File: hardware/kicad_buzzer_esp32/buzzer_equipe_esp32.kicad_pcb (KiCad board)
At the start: 2 copper layers, 110 x 125 mm, 6 parts, among them J2 Module charge TP4056+protect+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, J3 Module vibreur IN/VCC/GND, SW1 Bouton BUZZ (fils volants), SW2 Interrupteur marche/arret (fi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, U1 Vers ESP32 DevKit (module sur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

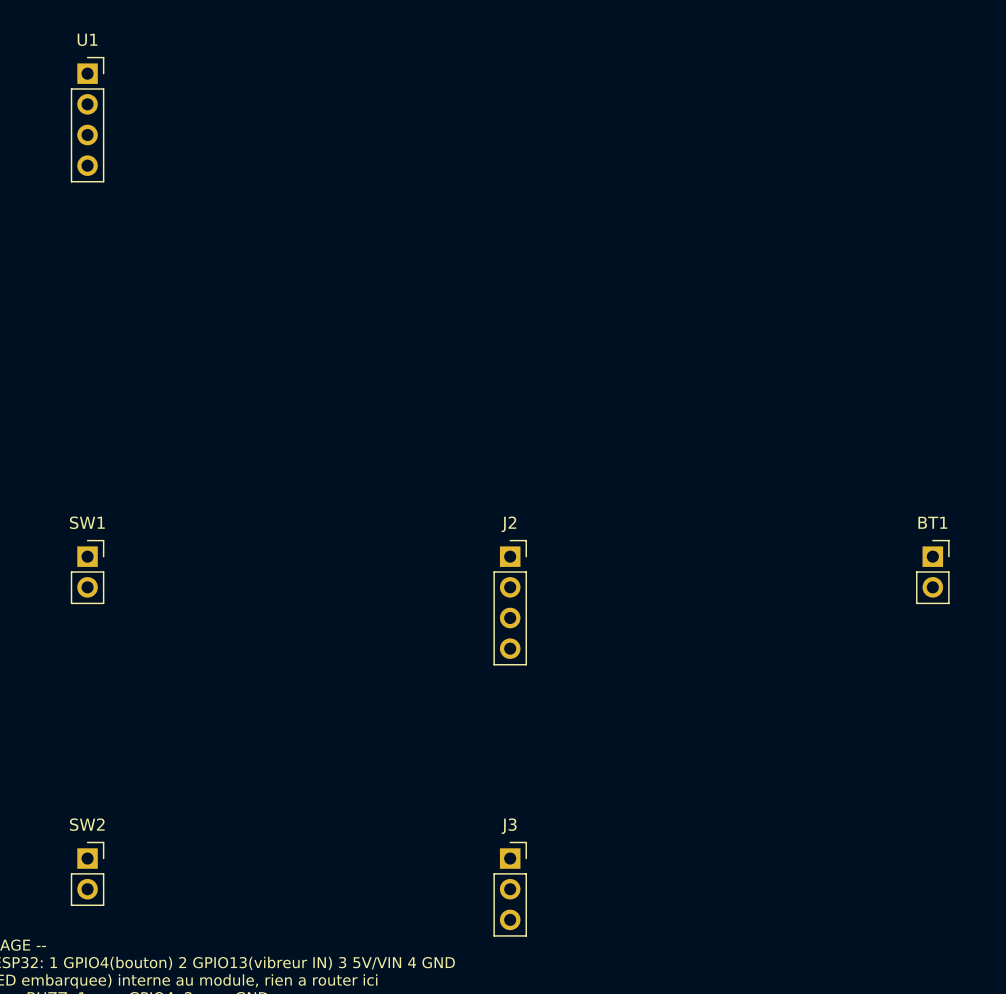
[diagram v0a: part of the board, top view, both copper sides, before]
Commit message: hardware: pistes routees sur les 3 cartes (Freerouting + kicad-cli pcb drc)
Autoroutage headless via Freerouting (pcbnew.ExportSpecctraDSN -> java -jar
freerouting.jar -> pcbnew.ImportSpecctraSES), pas un routage devine a la
main. Resultat verifie avec kicad-cli pcb drc reel sur les 3 cartes: 0
violation de clearance, 0 element non connecte. Seuls avertissements
restants: lib_footprint_mismatch (cosmetique) et quelques track_dangling
(residu mineur d'autorouter, a nettoyer dans KiCad, sans impact electrique).

Co-Authored-By: Claude Sonnet 5 <noreply@anthropic.com>
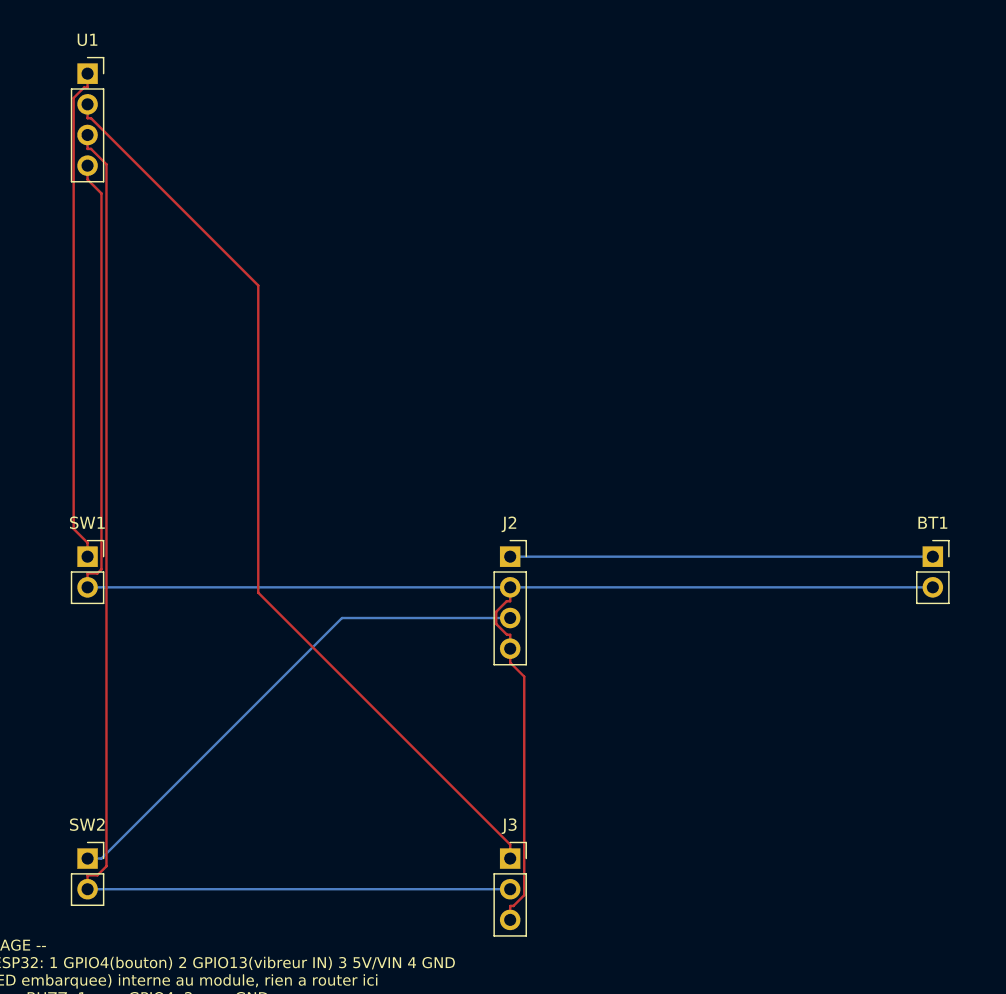
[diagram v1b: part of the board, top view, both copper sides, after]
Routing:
- net GND: track 0.00 -> 136.3 mm
- net VCC_5V_SW: track 0.00 -> 99.4 mm
- net VIBE_IN: track 0.00 -> 77.1 mm
- net VCC_5V_RAW: track 0.00 -> 43.3 mm
- net BTN_SIG: track 0.00 -> 41.1 mm
- net BAT_PLUS: track 0.00 -> 35.0 mm

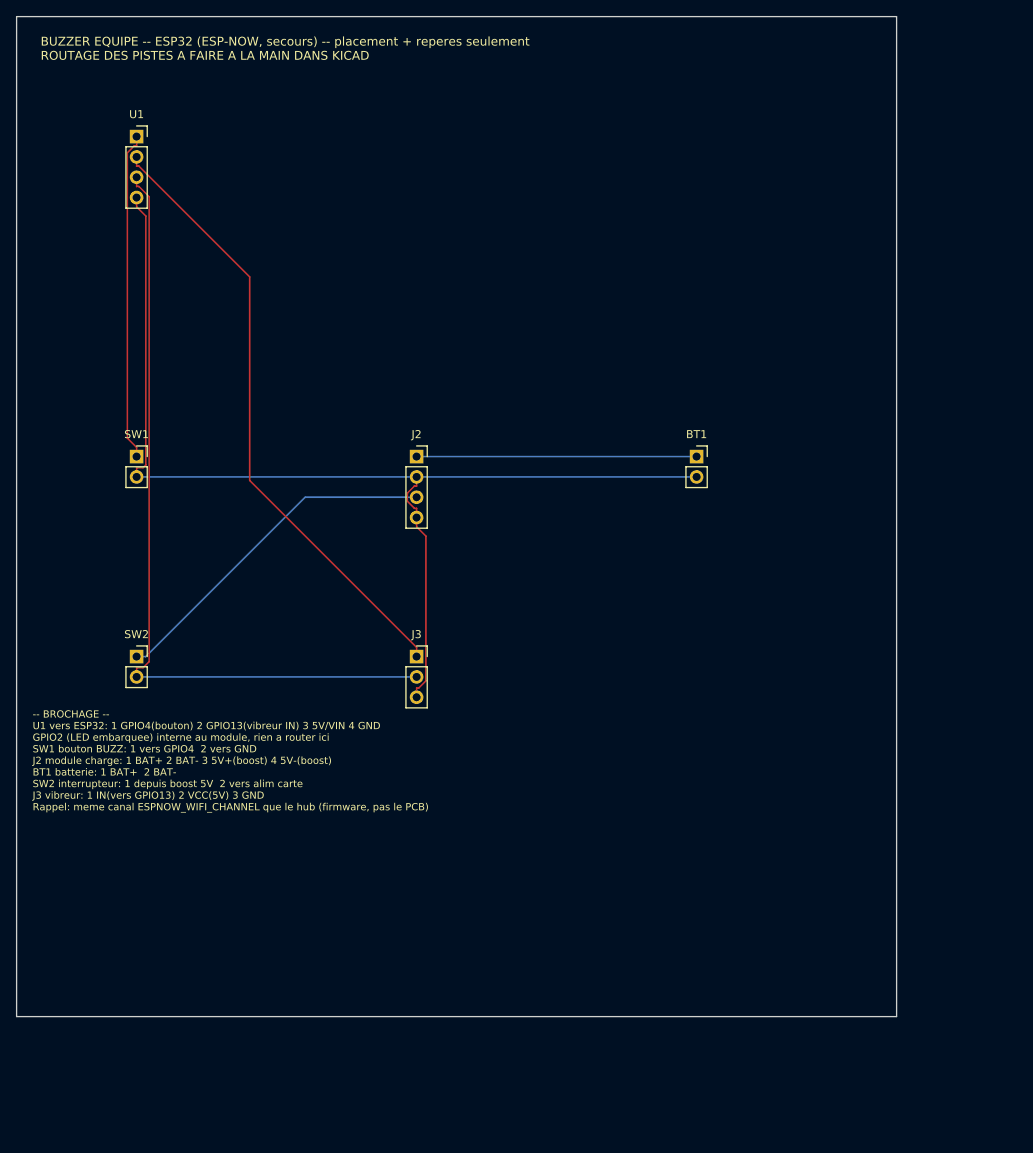
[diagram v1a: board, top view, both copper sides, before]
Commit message: hardware: vrais ports femelles pour les modules (Nano, ESP32 x2) + reroutage
Remplace les empreintes abstraites/simplifiees par de vraies barrettes
femelles PinSocket, dimensionnees et brochees pour correspondre aux modules
physiques reels, sur les 3 cartes:

- Nano (buzzer equipe): 2x PinSocket_1x15 (A1L/A1R, 30 broches, entraxe
  15,24mm) au lieu de l'empreinte "Nano soude directement" -- numerotation
  verifiee contre la vraie empreinte Module:Arduino_Nano.
- ESP32 buzzer (secours): 2x PinSocket_1x19 (U1L/U1R, 38 broches, entraxe
  22,86mm) au lieu du connecteur 4 broches abstrait -- brochage GPIO4/
  GPIO13/VIN/GND positionne selon le layout generique 38 broches le plus
  courant (verifie en ligne), avec avertissement clair dans le README:
  plusieurs variantes de clones existent, a verifier sur le module recu.
- ESP32 hub (regie): 2x PinSocket_1x15 (U_ESP32L/R, 30 broches, entraxe
  15,24mm) au lieu du connecteur 12 broches abstrait -- brochage DOIT ESP32
  DevKit V1 verifie (le modele exact confirme par le client), design de
  reference unique donc plus fiable que les clones 38 broches.

Les 34/19 broches physiques non utilisees sur chaque module restent
presentes sans net (fixation mecanique uniquement). Toutes les cartes
re-routees (Freerouting) et revalidees (kicad-cli pcb drc): 0 violation de
clearance, 0 element non connecte, 0 track_dangling restant (nettoyage
verifie topologie par topologie pour ne pas casser une piste utile).

Co-Authored-By: Claude Sonnet 5 <noreply@anthropic.com>
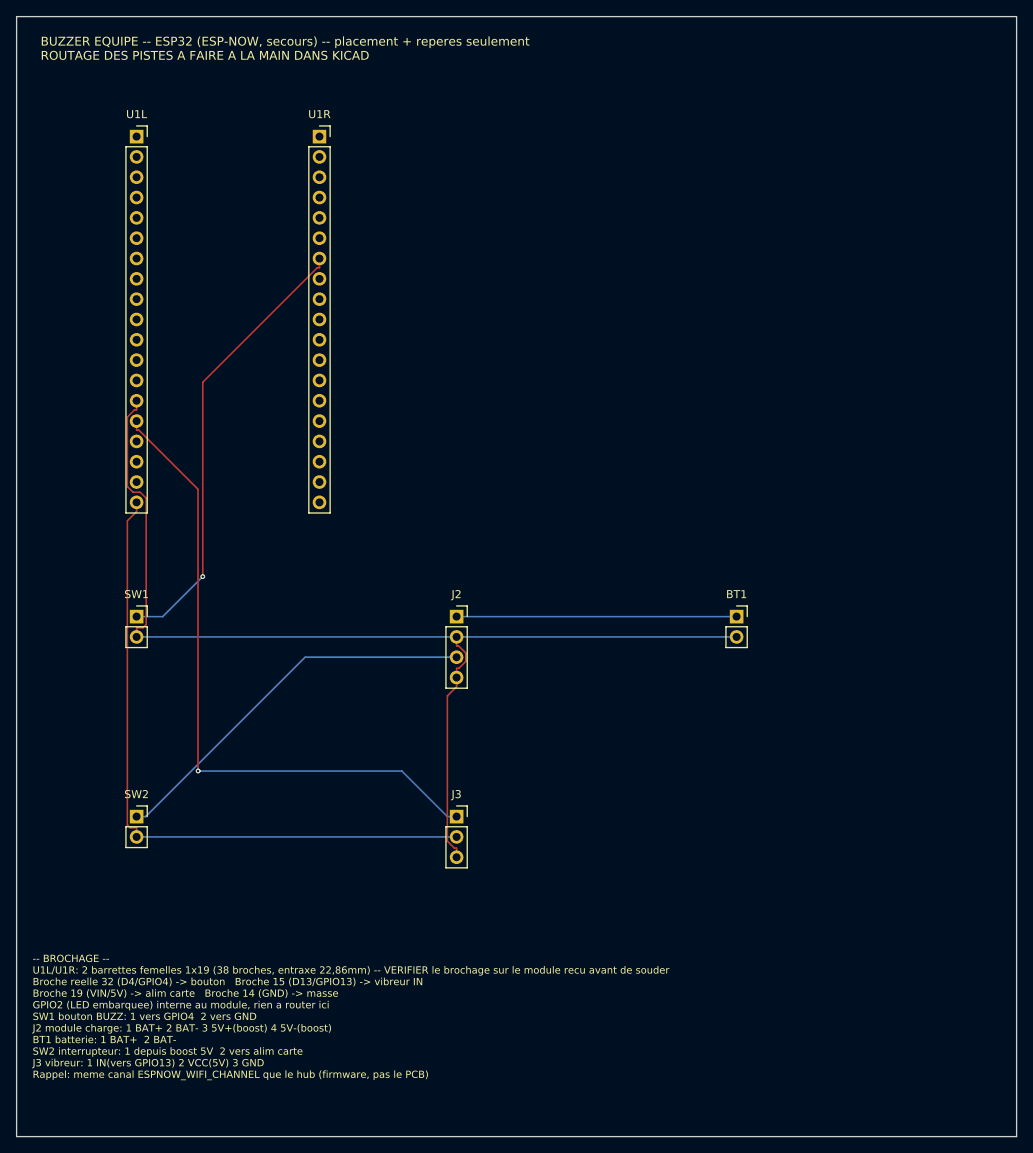
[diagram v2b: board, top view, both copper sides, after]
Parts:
- removed U1: Vers ESP32 DevKit (module sur headers femelles), Connector_PinSocket_2.54mm:PinSocket_1x04_P2.54mm_Vertical
- added U1L: ESP32 colonne gauche (broches 1-19) - VERIFIER sur le modul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, Connector_PinSocket_2.54mm:PinSocket_1x19_P2.54mm_Vertical, F.Cu at (20.0, 20.0)
- added U1R: ESP32 colonne droite (broches 20-38) - VERIFIER sur le modu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, Connector_PinSocket_2.54mm:PinSocket_1x19_P2.54mm_Vertical, F.Cu at (42.9, 20.0)
- moved BT1 20.6 mm to (95.0, 80.0)
- moved J2 20.6 mm to (60.0, 80.0)
- moved J3 20.6 mm to (60.0, 105.0)
- moved SW1 20.0 mm to (20.0, 80.0)
- moved SW2 20.0 mm to (20.0, 105.0)
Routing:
- net VCC_5V_SW: track 99.4 -> 83.3 mm
- net BTN_SIG: track 41.1 -> 56.3 mm, vias 0 -> 1
- net VCC_5V_RAW: track 43.3 -> 48.3 mm
- net VIBE_IN: track 77.1 -> 81.8 mm, vias 0 -> 1
- net GND: track 136.3 -> 137.6 mm
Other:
- board size 110 x 125 mm -> 125 x 140 mm
- board text added: "-- BROCHAGE -- U1L/U1R: 2 barrettes femelles 1x19 (38 broches, entraxe 22,86mm) -- VERIFIER le brochage sur le module recu avant de souder Broche reelle 32 (D4/GPIO4) -> bouton Broche 15 (D13/GPIO13) -> vibreur IN Broche 19 (VIN/5V) -> alim carte Broche 14 (GND) -> masse GPIO2 (LED embarquee) interne au module, rien a router ici SW1 bouton BUZZ: 1 vers GPIO4 2 vers GND J2 module charge: 1 BAT+ 2 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"
- board text removed: "-- BROCHAGE -- U1 vers ESP32: 1 GPIO4(bouton) 2 GPIO13(vibreur IN) 3 5V/VIN 4 GND GPIO2 (LED embarquee) interne au module, rien a router ici SW1 bouton BUZZ: 1 vers GPIO4 2 vers GND J2 module charge: 1 BAT+ 2 BAT- 3 5V+(boost) 4 5V-(boost) BT1 batterie: 1 BAT+ 2 BAT- SW2 interrupteur: 1 depuis boost 5V 2 vers alim carte J3 vibreur: 1 IN(vers GPIO13) 2 VCC(5V) 3 GND Rappel: meme canal ESPNOW_WIFI_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"

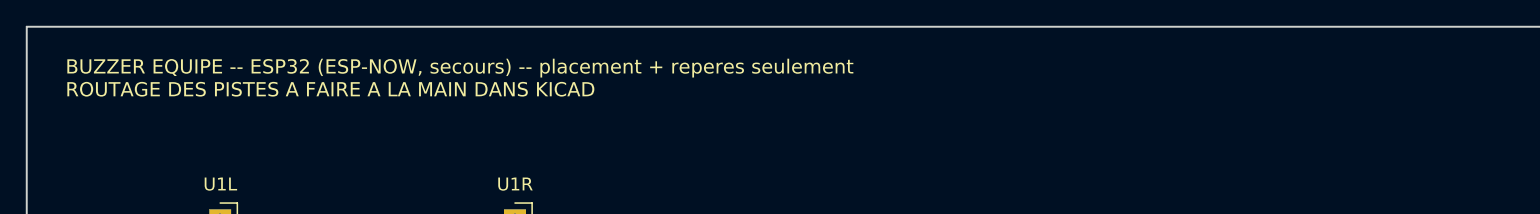
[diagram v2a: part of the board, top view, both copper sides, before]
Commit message: hardware: retire la mention "routage a faire a la main" (obsolete)
Le texte de titre sur la serigraphie des 3 cartes disait encore "ROUTAGE
DES PISTES A FAIRE A LA MAIN DANS KICAD", ecrit avant que le routage ne
soit fait via Freerouting. Remplace par une mention correcte ("pistes
routees (Freerouting), a relire avant fabrication"). Edition de texte
seule sur les fichiers deja routes -- aucune piste/pastille touchee,
DRC revalide identique (0 violation de clearance, 0 non connecte).

Co-Authored-By: Claude Sonnet 5 <noreply@anthropic.com>
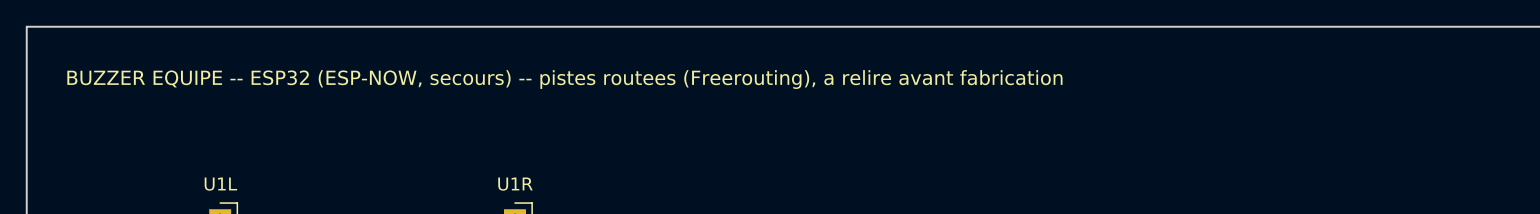
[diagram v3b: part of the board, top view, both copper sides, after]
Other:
- board text added: "BUZZER EQUIPE -- ESP32 (ESP-NOW, secours) -- pistes routees (Freerouting), a relire avant fabrication"
- board text removed: "BUZZER EQUIPE -- ESP32 (ESP-NOW, secours) -- placement + reperes seulement ROUTAGE DES PISTES A FAIRE A LA MAIN DANS KICAD"
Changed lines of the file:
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@@
 		)
 	)
-	(gr_text "BUZZER EQUIPE -- ESP32 (ESP-NOW, secours) -- placement + reperes seulement\nROUTAGE DES PISTES A FAIRE A LA MAIN DANS KICAD"
+	(gr_text "BUZZER EQUIPE -- ESP32 (ESP-NOW, secours) -- pistes routees (Freerouting), a relire avant fabrication"
 		(at 8 9 0)
 		(layer "F.SilkS")

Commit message: hardware: titres serigraphie simplifies (retire tout commentaire de process)
Le titre en haut de chaque carte disait encore des phrases du type "pistes
routees (Freerouting), a relire avant fabrication" -- du commentaire sur le
processus de generation, pas quelque chose qui a sa place gravee sur un vrai
circuit fabrique. Remplace par un simple nom de carte ("BUZZER EQUIPE -
NANO", "BUZZER EQUIPE - ESP32", "REGIE HUB"). Le bloc BROCHAGE (guide de
soudage demande explicitement) reste inchange. Edition de texte seule,
DRC revalide identique sur les 3 cartes.

Co-Authored-By: Claude Sonnet 5 <noreply@anthropic.com>
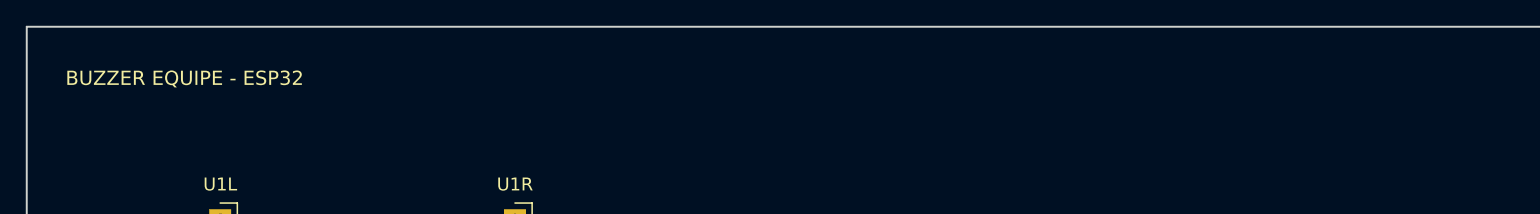
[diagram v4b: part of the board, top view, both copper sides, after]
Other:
- board text added: "BUZZER EQUIPE - ESP32"
- board text removed: "BUZZER EQUIPE -- ESP32 (ESP-NOW, secours) -- pistes routees (Freerouting), a relire avant fabrication"
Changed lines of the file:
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@@
 		)
 	)
-	(gr_text "BUZZER EQUIPE -- ESP32 (ESP-NOW, secours) -- pistes routees (Freerouting), a relire avant fabrication"
+	(gr_text "BUZZER EQUIPE - ESP32"
 		(at 8 9 0)
 		(layer "F.SilkS")
